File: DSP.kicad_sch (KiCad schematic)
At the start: 24 parts, among them J2 Conn_01x04, J3 MEM2067-02-180-00-A_REVB, J5 Conn_01x04, U4 STM32F401RBTx, Y1 16MHz

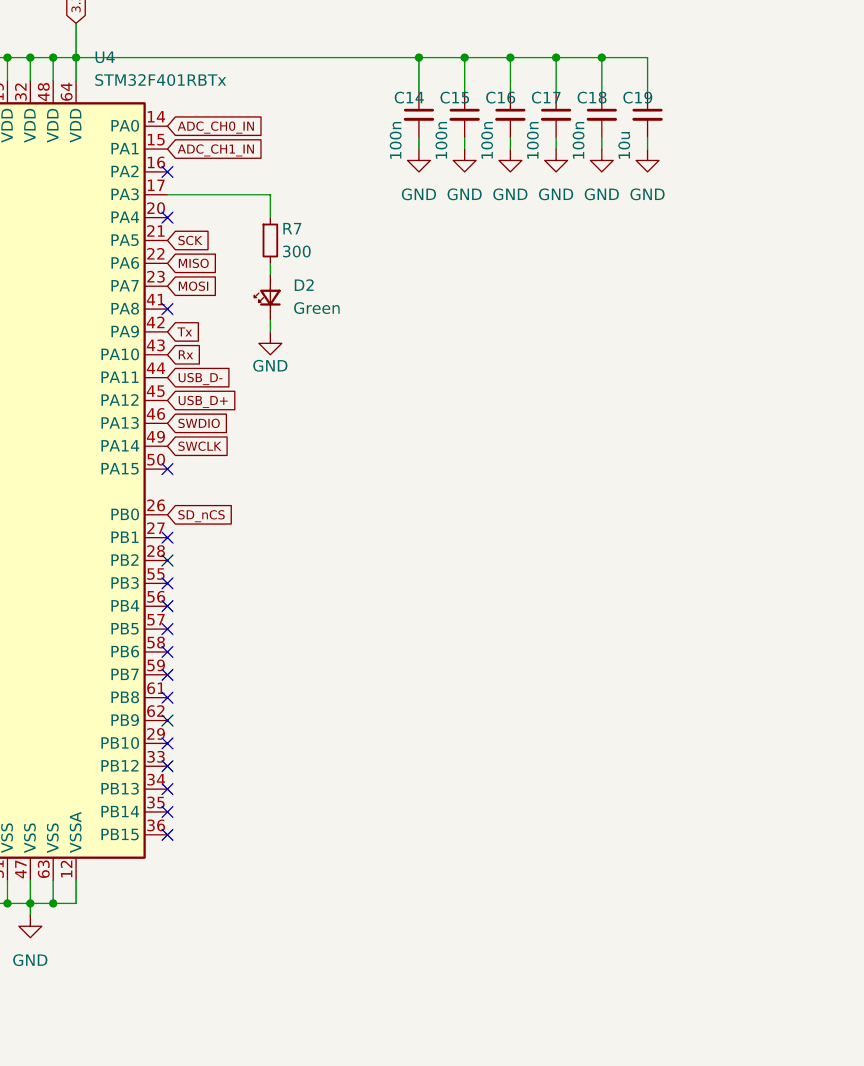
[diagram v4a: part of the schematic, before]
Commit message: added sram chip again, might come in handy for mor complex calculations
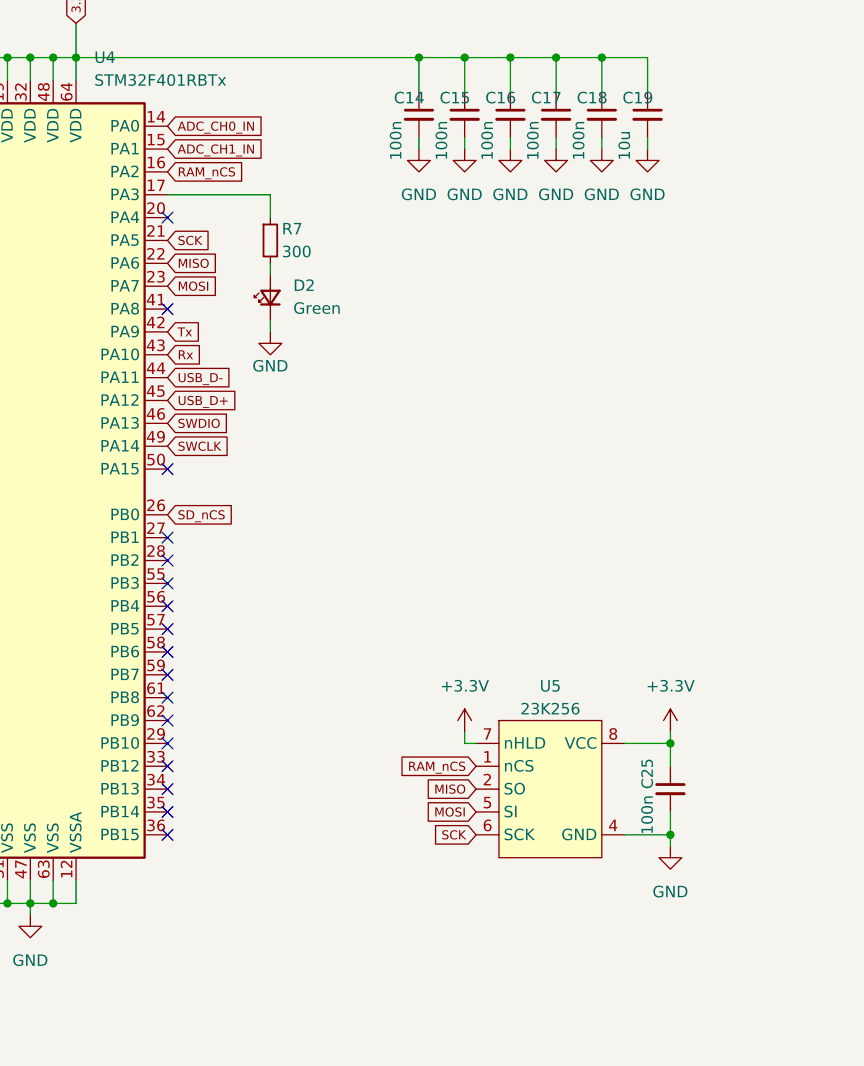
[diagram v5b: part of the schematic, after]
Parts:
- added C25: 100n, Capacitor_SMD:C_0603_1608Metric_Pad1.08x0.95mm_HandSolder, symbol Device:C_Small
- added U5: 23K256, Package_SO:SOIC-8_3.9x4.9mm_P1.27mm, symbol 23K256:23K256
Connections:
- net +3V3: now also C25.1, U5.7 (nHLD), U5.8 (VCC)
- net GND: now also C25.2, U5.4 (GND)
- net MISO: now also U5.2 (SO)
- net MOSI: now also U5.5 (SI)
- net SCK: now also U5.6 (SCK)
- net RAM_nCS: now reaches U4.16 (PA2)
- net RAM_nCS: now also U5.1 (nCS)
- no-connect marks 38 -> 37
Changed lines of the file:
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@@
   (junction (at 111.76 34.29) (diameter 0) (color 0 0 0 0)
   )
+  (junction (at 185.42 110.49) (diameter 0) (color 0 0 0 0)
+  )
   (junction (at 53.34 177.8) (diameter 0) (color 0 0 0 0)
   )
@@
   )
   (junction (at 109.22 34.29) (diameter 0) (color 0 0 0 0)
+  )
+  (junction (at 185.42 120.65) (diameter 0) (color 0 0 0 0)
   )
   (junction (at 119.38 34.29) (diameter 0) (color 0 0 0 0)
@@
   (no_connect (at 96.52 102.87))
   (no_connect (at 129.54 87.63))
-  (no_connect (at 129.54 46.99))
   (no_connect (at 96.52 85.09))
   (no_connect (at 129.54 62.23))
@@
     (stroke (width 0) (type default))
   )
+  (wire (pts (xy 185.42 120.65) (xy 180.34 120.65))
+    (stroke (width 0) (type default))
+  )
   (wire (pts (xy 92.71 58.42) (xy 92.71 59.69))
     (stroke (width 0) (type default))
@@
     (stroke (width 0) (type default))
   )
+  (wire (pts (xy 185.42 118.11) (xy 185.42 120.65))
+    (stroke (width 0) (type default))
+  )
   (wire (pts (xy 172.72 43.18) (xy 172.72 44.45))
     (stroke (width 0) (type default))
@@
     (stroke (width 0) (type default))
   )
+  (wire (pts (xy 185.42 120.65) (xy 185.42 121.92))
+    (stroke (width 0) (type default))
+  )
   (wire (pts (xy 111.76 34.29) (xy 111.76 36.83))
     (stroke (width 0) (type default))
@@
     (stroke (width 0) (type default))
   )
+  (wire (pts (xy 185.42 110.49) (xy 180.34 110.49))
+    (stroke (width 0) (type default))
+  )
   (wire (pts (xy 53.34 168.91) (xy 48.26 168.91))
     (stroke (width 0) (type default))
@@
     (stroke (width 0) (type default))
   )
+  (wire (pts (xy 185.42 113.03) (xy 185.42 110.49))
+    (stroke (width 0) (type default))
+  )
   (wire (pts (xy 214.63 99.06) (xy 215.9 99.06))
     (stroke (width 0) (type default))
@@
     (stroke (width 0) (type default))
   )
+  (wire (pts (xy 162.56 110.49) (xy 163.83 110.49))
+    (stroke (width 0) (type default))
+  )
   (wire (pts (xy 53.34 172.72) (xy 69.85 172.72))
     (stroke (width 0) (type default))
@@
     (stroke (width 0) (type default))
   )
+  (wire (pts (xy 185.42 109.22) (xy 185.42 110.49))
+    (stroke (width 0) (type default))
+  )
   (wire (pts (xy 177.8 38.1) (xy 177.8 34.29))
     (stroke (width 0) (type default))
@@
   )
   (wire (pts (xy 60.96 36.83) (xy 67.31 36.83))
+    (stroke (width 0) (type default))
+  )
+  (wire (pts (xy 162.56 109.22) (xy 162.56 110.49))
     (stroke (width 0) (type default))
   )
@@
     )
   )
+  (global_label "MISO" (shape input) (at 163.83 115.57 180) (fields_autoplaced)
+    (effects (font (size 1 1)) (justify right))
+    (property "Intersheetrefs" "${INTERSHEET_REFS}" (at 157.923 115.57 0)
+      (effects (font (size 1 1)) (justify right) hide)
+    )
+  )
+  (global_label "RAM_nCS" (shape input) (at 129.54 46.99 0) (fields_autoplaced)
+    (effects (font (size 1 1)) (justify left))
+    (property "Intersheetrefs" "${INTERSHEET_REFS}" (at 138.447 46.99 0)
+      (effects (font (size 1 1)) (justify left) hide)
+    )
+  )
   (global_label "SWCLK" (shape input) (at 129.54 77.47 0) (fields_autoplaced)
     (effects (font (size 1 1)) (justify left))
@@
     )
   )
+  (global_label "SCK" (shape input) (at 163.83 120.65 180) (fields_autoplaced)
+    (effects (font (size 1 1)) (justify right))
+    (property "Intersheetrefs" "${INTERSHEET_REFS}" (at 158.5897 120.65 0)
+      (effects (font (size 1 1)) (justify right) hide)
+    )
+  )
   (global_label "SWDIO" (shape input) (at 129.54 74.93 0) (fields_autoplaced)
     (effects (font (size 1 1)) (justify left))
@@
     )
   )
+  (global_label "MOSI" (shape input) (at 163.83 118.11 180) (fields_autoplaced)
+    (effects (font (size 1 1)) (justify right))
+    (property "Intersheetrefs" "${INTERSHEET_REFS}" (at 157.923 118.11 0)
+      (effects (font (size 1 1)) (justify right) hide)
+    )
+  )
   (global_label "3.3V" (shape input) (at 119.38 30.48 90) (fields_autoplaced)
     (effects (font (size 1 1)) (justify left))
@@
     )
   )
+  (global_label "RAM_nCS" (shape input) (at 163.83 113.03 180) (fields_autoplaced)
+    (effects (font (size 1 1)) (justify right))
+    (property "Intersheetrefs" "${INTERSHEET_REFS}" (at 154.923 113.03 0)
+      (effects (font (size 1 1)) (justify right) hide)
+    )
+  )
   (global_label "MOSI" (shape input) (at 69.85 167.64 180) (fields_autoplaced)
     (effects (font (size 1 1)) (justify right))
@@
         (path "/e63e39d7-6ac0-4ffd-8aa3-1841a4541b55/65c41d2a-7921-40f6-8a66-43d43155f96a"
           (reference "BOOT1") (unit 1)
+        )
+      )
+    )
+  )
+  (symbol (lib_id "Device:C_Small") (at 185.42 115.57 0) (unit 1)
+    (in_bom yes) (on_board yes) (dnp no)
+    (property "Reference" "C25" (at 182.88 115.57 90)
+      (effects (font (size 1.27 1.27)) (justify left))
+    )
+    (property "Value" "100n" (at 182.88 120.65 90)
+      (effects (font (size 1.27 1.27)) (justify left))
+    )
+    (property "Footprint" "Capacitor_SMD:C_0603_1608Metric_Pad1.08x0.95mm_HandSolder" (at 185.42 115.57 0)
+      (effects (font (size 1.27 1.27)) hide)
+    )
+    (property "Datasheet" "~" (at 185.42 115.57 0)
+      (effects (font (size 1.27 1.27)) hide)
+    )
+    (pin "1")
+    (pin "2")
+    (instances
+      (project "Apollo - DSP"
+        (path "/e63e39d7-6ac0-4ffd-8aa3-1841a4541b55/65c41d2a-7921-40f6-8a66-43d43155f96a"
+          (reference "C25") (unit 1)
         )
       )
@@
     )
   )
+  (symbol (lib_id "power:GND") (at 185.42 121.92 0) (unit 1)
+    (in_bom yes) (on_board yes) (dnp no) (fields_autoplaced)
+    (property "Reference" "#PWR010" (at 185.42 128.27 0)
+      (effects (font (size 1.27 1.27)) hide)
+    )
+    (property "Value" "GND" (at 185.42 127 0)
+      (effects (font (size 1.27 1.27)))
+    )
+    (property "Footprint" "" (at 185.42 121.92 0)
+      (effects (font (size 1.27 1.27)) hide)
+    )
+    (property "Datasheet" "" (at 185.42 121.92 0)
+      (effects (font (size 1.27 1.27)) hide)
+    )
+    (pin "1")
+    (instances
+      (project "Apollo - DSP"
+        (path "/e63e39d7-6ac0-4ffd-8aa3-1841a4541b55/65c41d2a-7921-40f6-8a66-43d43155f96a"
+          (reference "#PWR010") (unit 1)
+        )
+      )
+    )
+  )
   (symbol (lib_id "Device:C_Small") (at 157.48 40.64 0) (unit 1)
     (in_bom yes) (on_board yes) (dnp no)
@@
     )
   )
+  (symbol (lib_id "power:+3.3V") (at 162.56 109.22 0) (unit 1)
+    (in_bom yes) (on_board yes) (dnp no) (fields_autoplaced)
+    (property "Reference" "#PWR011" (at 162.56 113.03 0)
+      (effects (font (size 1.27 1.27)) hide)
+    )
+    (property "Value" "+3.3V" (at 162.56 104.14 0)
+      (effects (font (size 1.27 1.27)))
+    )
+    (property "Footprint" "" (at 162.56 109.22 0)
+      (effects (font (size 1.27 1.27)) hide)
+    )
+    (property "Datasheet" "" (at 162.56 109.22 0)
+      (effects (font (size 1.27 1.27)) hide)
+    )
+    (pin "1")
+    (instances
+      (project "Apollo - DSP"
+        (path "/e63e39d7-6ac0-4ffd-8aa3-1841a4541b55/65c41d2a-7921-40f6-8a66-43d43155f96a"
+          (reference "#PWR011") (unit 1)
+        )
+      )
+    )
+  )
   (symbol (lib_id "Device:R_Small") (at 140.97 54.61 0) (unit 1)
     (in_bom yes) (on_board yes) (dnp no)
@@
     )
   )
+  (symbol (lib_id "power:+3.3V") (at 185.42 109.22 0) (unit 1)
+    (in_bom yes) (on_board yes) (dnp no) (fields_autoplaced)
+    (property "Reference" "#PWR09" (at 185.42 113.03 0)
+      (effects (font (size 1.27 1.27)) hide)
+    )
+    (property "Value" "+3.3V" (at 185.42 104.14 0)
+      (effects (font (size 1.27 1.27)))
+    )
+    (property "Footprint" "" (at 185.42 109.22 0)
+      (effects (font (size 1.27 1.27)) hide)
+    )
+    (property "Datasheet" "" (at 185.42 109.22 0)
+      (effects (font (size 1.27 1.27)) hide)
+    )
+    (pin "1")
+    (instances
+      (project "Apollo - DSP"
+        (path "/e63e39d7-6ac0-4ffd-8aa3-1841a4541b55/65c41d2a-7921-40f6-8a66-43d43155f96a"
+          (reference "#PWR09") (unit 1)
+        )
+      )
+    )
+  )
   (symbol (lib_id "power:GND") (at 177.8 44.45 0) (unit 1)
     (in_bom yes) (on_board yes) (dnp no) (fields_autoplaced)
@@
         )
       )
+    )
+  )
+  (symbol (lib_id "23K256:23K256") (at 171.45 123.19 0) (unit 1)
+    (in_bom yes) (on_board yes) (dnp no) (fields_autoplaced)
+    (property "Reference" "U5" (at 172.085 104.14 0)
+      (effects (font (size 1.27 1.27)))
+    )
+    (property "Value" "23K256" (at 172.085 106.68 0)
+      (effects (font (size 1.27 1.27)))
+    )
+    (property "Footprint" "Package_SO:SOIC-8_3.9x4.9mm_P1.27mm" (at 170.18 104.14 0)
+      (effects (font (size 1.27 1.27)) hide)
+    )
+    (property "Datasheet" "https://ww1.microchip.com/downloads/en/DeviceDoc/22100F.pdf" (at 170.18 104.14 0)
+      (effects (font (size 1.27 1.27)) hide)
+    )
+    (pin "1")
+    (pin "2")
+    (pin "3")
+    (pin "4")
+    (pin "5")
+    (pin "6")
+    (pin "7")
+    (pin "8")
+    (instances
+      (project "Apollo - DSP"
+        (path "/e63e39d7-6ac0-4ffd-8aa3-1841a4541b55/65c41d2a-7921-40f6-8a66-43d43155f96a"
+          (reference "U5") (unit 1)
+        )
+      )

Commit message: updated pics
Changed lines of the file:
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@@
   (no_connect (at 96.52 107.95))
   (no_connect (at 129.54 120.65))
+  (bus_entry (at 203.2 10.16) (size 2.54 2.54)
+    (stroke (width 0) (type default))
+  )
   (wire (pts (xy 64.77 93.98) (xy 64.77 96.52))
     (stroke (width 0) (type default))

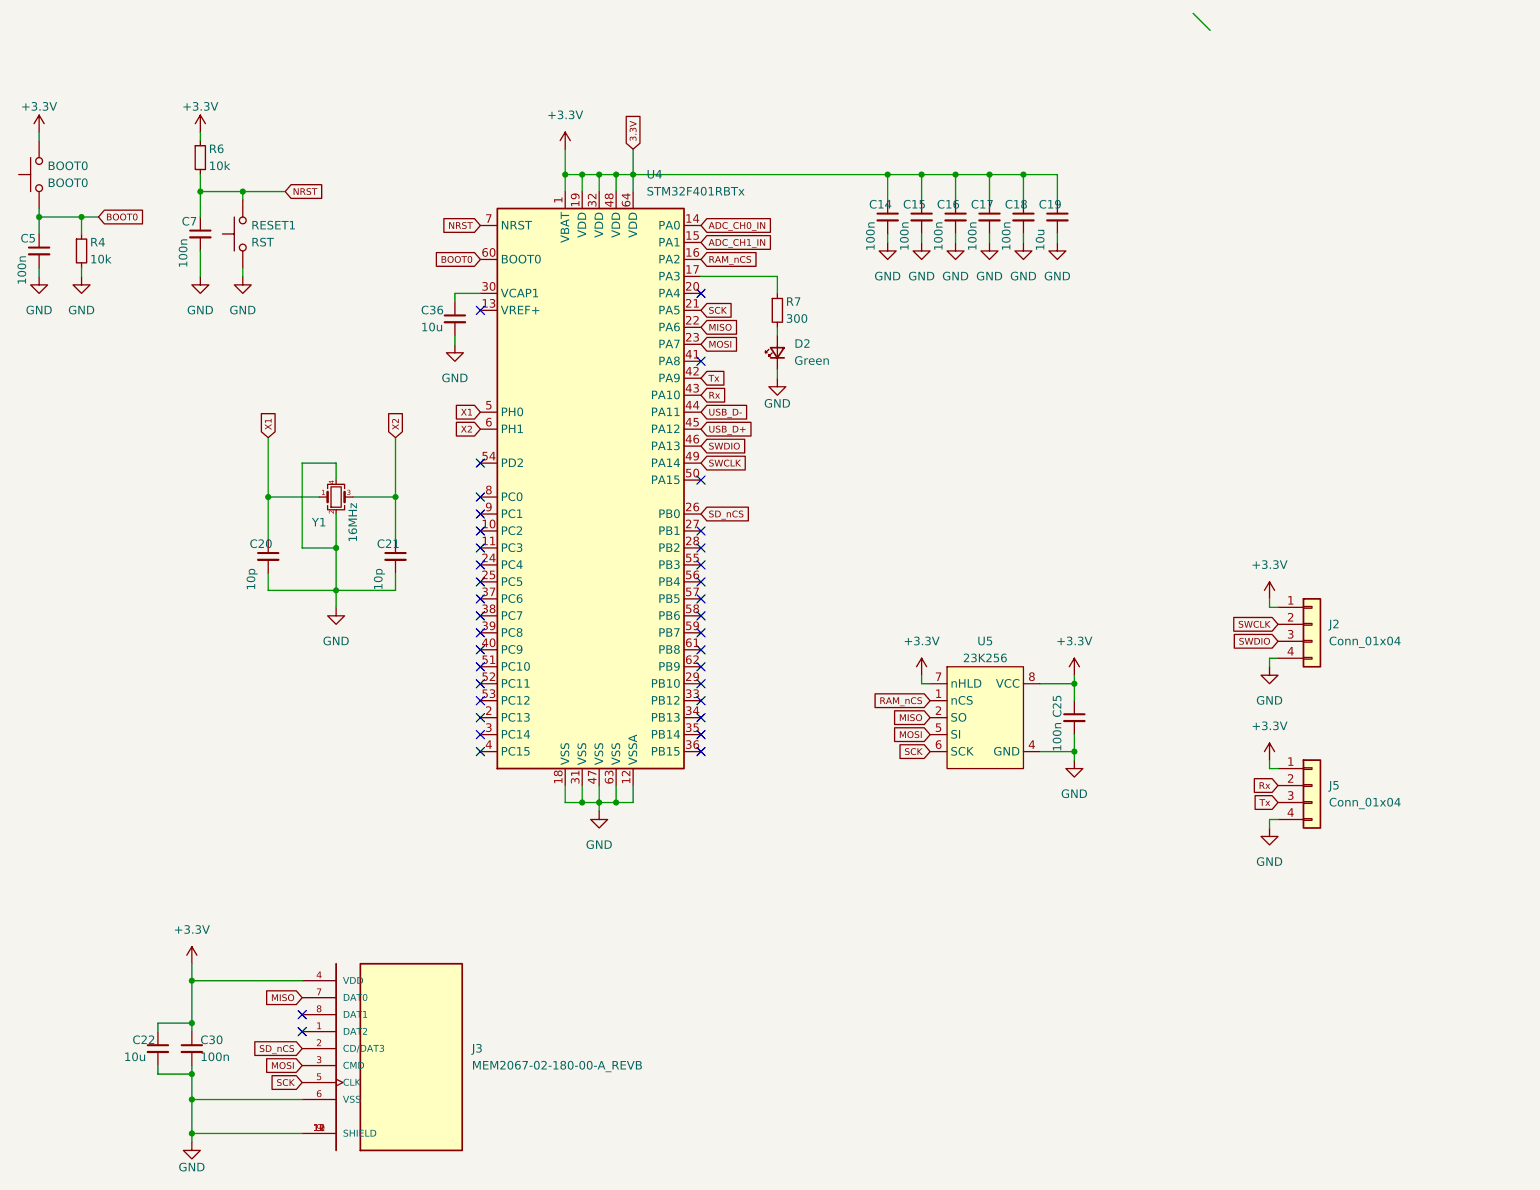
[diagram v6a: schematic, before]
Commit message: added DAC and an onboard fixed oscilltor to quickly test the DSP
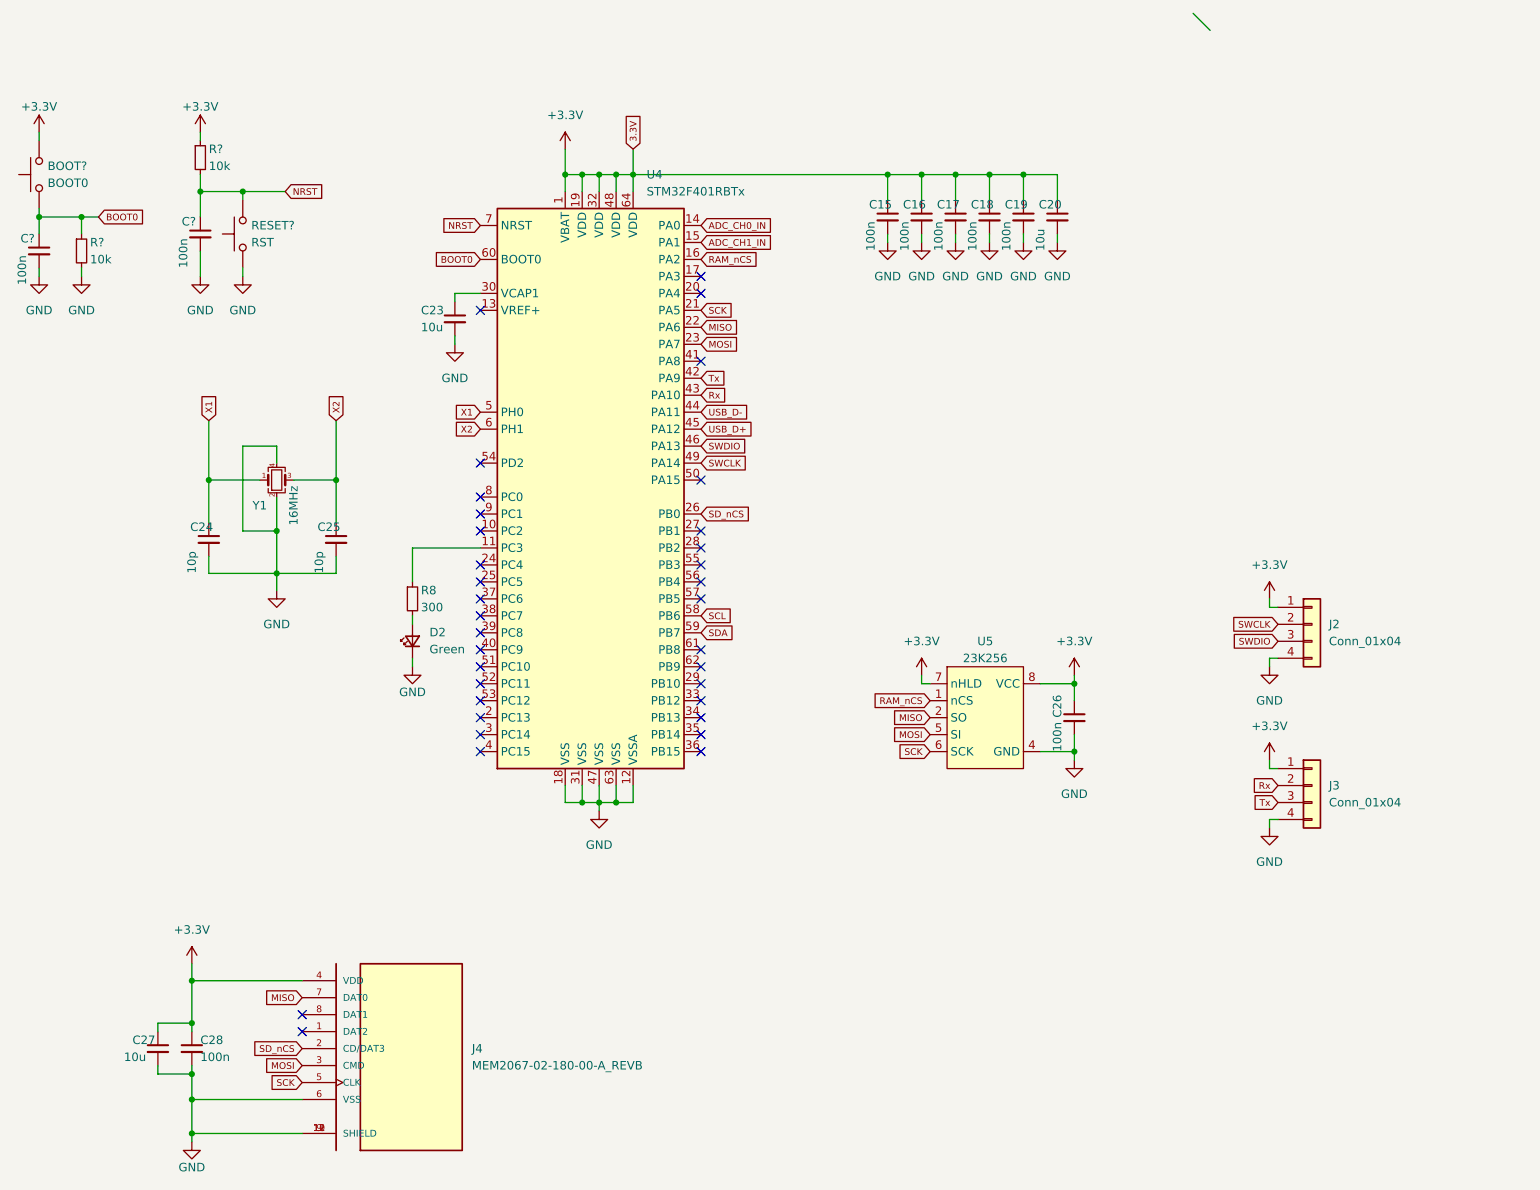
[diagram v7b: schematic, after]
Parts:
- renumbered BOOT0 to BOOT?, C14 to C15, C15 to C16, C16 to C17, C17 to C18, C18 to C19, C19 to C20, C36 to C23, C20 to C24, C21 to C25, C25 to C26, C22 to C27, C30 to C28, C5 to C?, C7 to C?, J5 to J3, J3 to J4, R7 to R8, R6 to R?, R4 to R?, RESET1 to RESET?
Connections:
- net at R8.1: now also U4.11 (PC3); no longer U4.17 (PA3)
- net SCL: now reaches U4.58 (PB6)
- net SDA: now reaches U4.59 (PB7)
- no-connect marks 37 -> 35
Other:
- moved on the sheet: C24, C25, D2, R8, Y1
